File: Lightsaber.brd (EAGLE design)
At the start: 210 x 10 mm, 25 parts

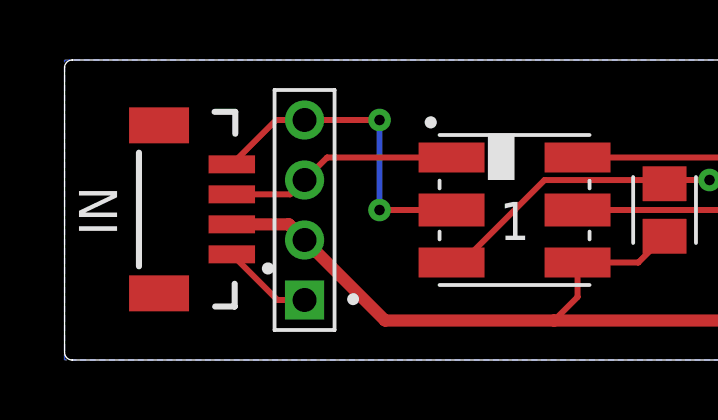
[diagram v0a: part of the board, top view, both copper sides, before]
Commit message: Fix ground trace width
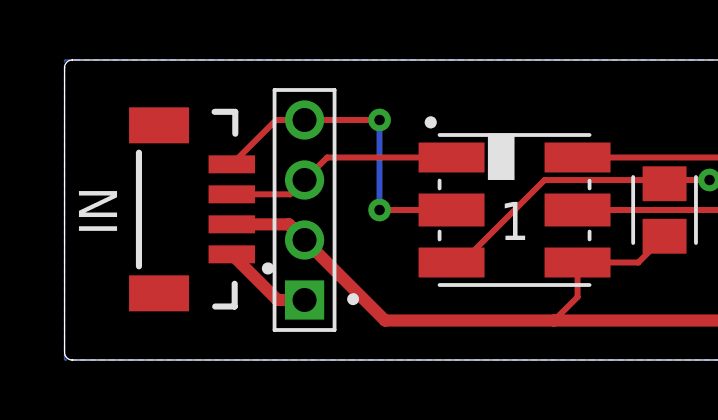
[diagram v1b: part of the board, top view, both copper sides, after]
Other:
- board text added: "Lightsaber V1.2 @0x76656e"
- board text removed: "Lightsaber V1.1 @0x76656e"
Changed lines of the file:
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@@
 <layer number="14" name="Route14" color="1" fill="6" visible="no" active="no"/>
 <layer number="15" name="Route15" color="4" fill="6" visible="no" active="no"/>
-<layer number="16" name="Bottom" color="1" fill="1" visible="yes" active="yes"/>
+<layer number="16" name="Bottom" color="1" fill="1" visible="no" active="yes"/>
 <layer number="17" name="Pads" color="2" fill="1" visible="yes" active="yes"/>
 <layer number="18" name="Vias" color="2" fill="1" visible="yes" active="yes"/>
@@
 <layer number="20" name="Dimension" color="24" fill="1" visible="yes" active="yes"/>
 <layer number="21" name="tPlace" color="7" fill="1" visible="yes" active="yes"/>
-<layer number="22" name="bPlace" color="7" fill="1" visible="yes" active="yes"/>
+<layer number="22" name="bPlace" color="7" fill="1" visible="no" active="yes"/>
 <layer number="23" name="tOrigins" color="15" fill="1" visible="yes" active="yes"/>
-<layer number="24" name="bOrigins" color="15" fill="1" visible="yes" active="yes"/>
+<layer number="24" name="bOrigins" color="15" fill="1" visible="no" active="yes"/>
 <layer number="25" name="tNames" color="7" fill="1" visible="yes" active="yes"/>
-<layer number="26" name="bNames" color="7" fill="1" visible="yes" active="yes"/>
+<layer number="26" name="bNames" color="7" fill="1" visible="no" active="yes"/>
 <layer number="27" name="tValues" color="7" fill="1" visible="no" active="yes"/>
 <layer number="28" name="bValues" color="7" fill="1" visible="no" active="yes"/>
@@
 <layer number="38" name="bTest" color="7" fill="1" visible="no" active="yes"/>
 <layer number="39" name="tKeepout" color="4" fill="11" visible="yes" active="yes"/>
-<layer number="40" name="bKeepout" color="1" fill="11" visible="yes" active="yes"/>
+<layer number="40" name="bKeepout" color="1" fill="11" visible="no" active="yes"/>
 <layer number="41" name="tRestrict" color="4" fill="10" visible="yes" active="yes"/>
-<layer number="42" name="bRestrict" color="1" fill="10" visible="yes" active="yes"/>
+<layer number="42" name="bRestrict" color="1" fill="10" visible="no" active="yes"/>
 <layer number="43" name="vRestrict" color="2" fill="10" visible="no" active="yes"/>
 <layer number="44" name="Drills" color="7" fill="1" visible="no" active="yes"/>
@@
 <layer number="50" name="dxf" color="7" fill="1" visible="no" active="no"/>
 <layer number="51" name="tDocu" color="7" fill="1" visible="yes" active="yes"/>
-<layer number="52" name="bDocu" color="7" fill="1" visible="yes" active="yes"/>
+<layer number="52" name="bDocu" color="7" fill="1" visible="no" active="yes"/>
 <layer number="53" name="tGND_GNDA" color="7" fill="9" visible="no" active="no"/>
 <layer number="54" name="bGND_GNDA" color="1" fill="9" visible="no" active="no"/>
@@
 <rectangle x1="194.05" y1="9.25" x2="194.35" y2="9.35" layer="22" rot="R180"/>
 <rectangle x1="191.25" y1="9.25" x2="193.65" y2="9.35" layer="22" rot="R180"/>
-<text x="180.5" y="2.8" size="1.778" layer="22" font="vector" ratio="10" rot="MR0">Lightsaber V1.1
+<text x="180.5" y="2.8" size="1.778" layer="22" font="vector" ratio="10" rot="MR0">Lightsaber V1.2
 @0x76656e</text>
 <text x="5" y="1.5" size="1.016" layer="22" font="vector" rot="MR0">GND</text>
@@
 <contactref element="OUT" pad="1"/>
 <contactref element="IN" pad="1"/>
-<wire x1="5.575" y1="3.522" x2="7.097" y2="2" width="0.2" layer="1"/>
-<wire x1="7.097" y1="2" x2="8" y2="2" width="0.2" layer="1"/>
+<wire x1="5.575" y1="3.522" x2="7.097" y2="2" width="0.4064" layer="1"/>
+<wire x1="7.097" y1="2" x2="8" y2="2" width="0.4064" layer="1"/>
 <contactref element="H1" pad="B2,8"/>
 <contactref element="H2" pad="B2,8"/>
+<wire x1="201.5" y1="6" x2="207" y2="2" width="0" layer="19" extent="1-1"/>
+<wire x1="186" y1="5" x2="192.9" y2="3.25" width="0" layer="19" extent="1-1"/>
+<wire x1="181.5" y1="6" x2="186" y2="5" width="0" layer="19" extent="1-1"/>
+<wire x1="161.5" y1="6" x2="172.9" y2="3.25" width="0" layer="19" extent="1-1"/>
+<wire x1="141.5" y1="6" x2="152.9" y2="3.25" width="0" layer="19" extent="1-1"/>
+<wire x1="121.5" y1="6" x2="132.9" y2="3.25" width="0" layer="19" extent="1-1"/>
+<wire x1="101.5" y1="6" x2="112.9" y2="3.25" width="0" layer="19" extent="1-1"/>
+<wire x1="81.5" y1="6" x2="92.9" y2="3.25" width="0" layer="19" extent="1-1"/>
+<wire x1="61.5" y1="6" x2="72.9" y2="3.25" width="0" layer="19" extent="1-1"/>
+<wire x1="41.5" y1="6" x2="52.9" y2="3.25" width="0" layer="19" extent="1-1"/>
+<wire x1="26" y1="5" x2="32.9" y2="3.25" width="0" layer="19" extent="1-1"/>
+<wire x1="21.5" y1="6" x2="26" y2="5" width="0" layer="19" extent="1-1"/>
+<wire x1="8" y1="2" x2="12.9" y2="3.25" width="0" layer="19" extent="1-1"/>
 </signal>
 <signal name="VCC">
